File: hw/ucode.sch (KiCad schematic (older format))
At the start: 15 parts, among them U501 74HC393, U502 74HCT02, U503 74HCT02, U504 74HCT238, U505 74HCT238, U506 27C64, U507 27C64, U508 27C64, U509 74HCT175, U510 74HCT175, U511 74HCT175, U512 74HCT175, U513 74HCT175, U514 74HCT175

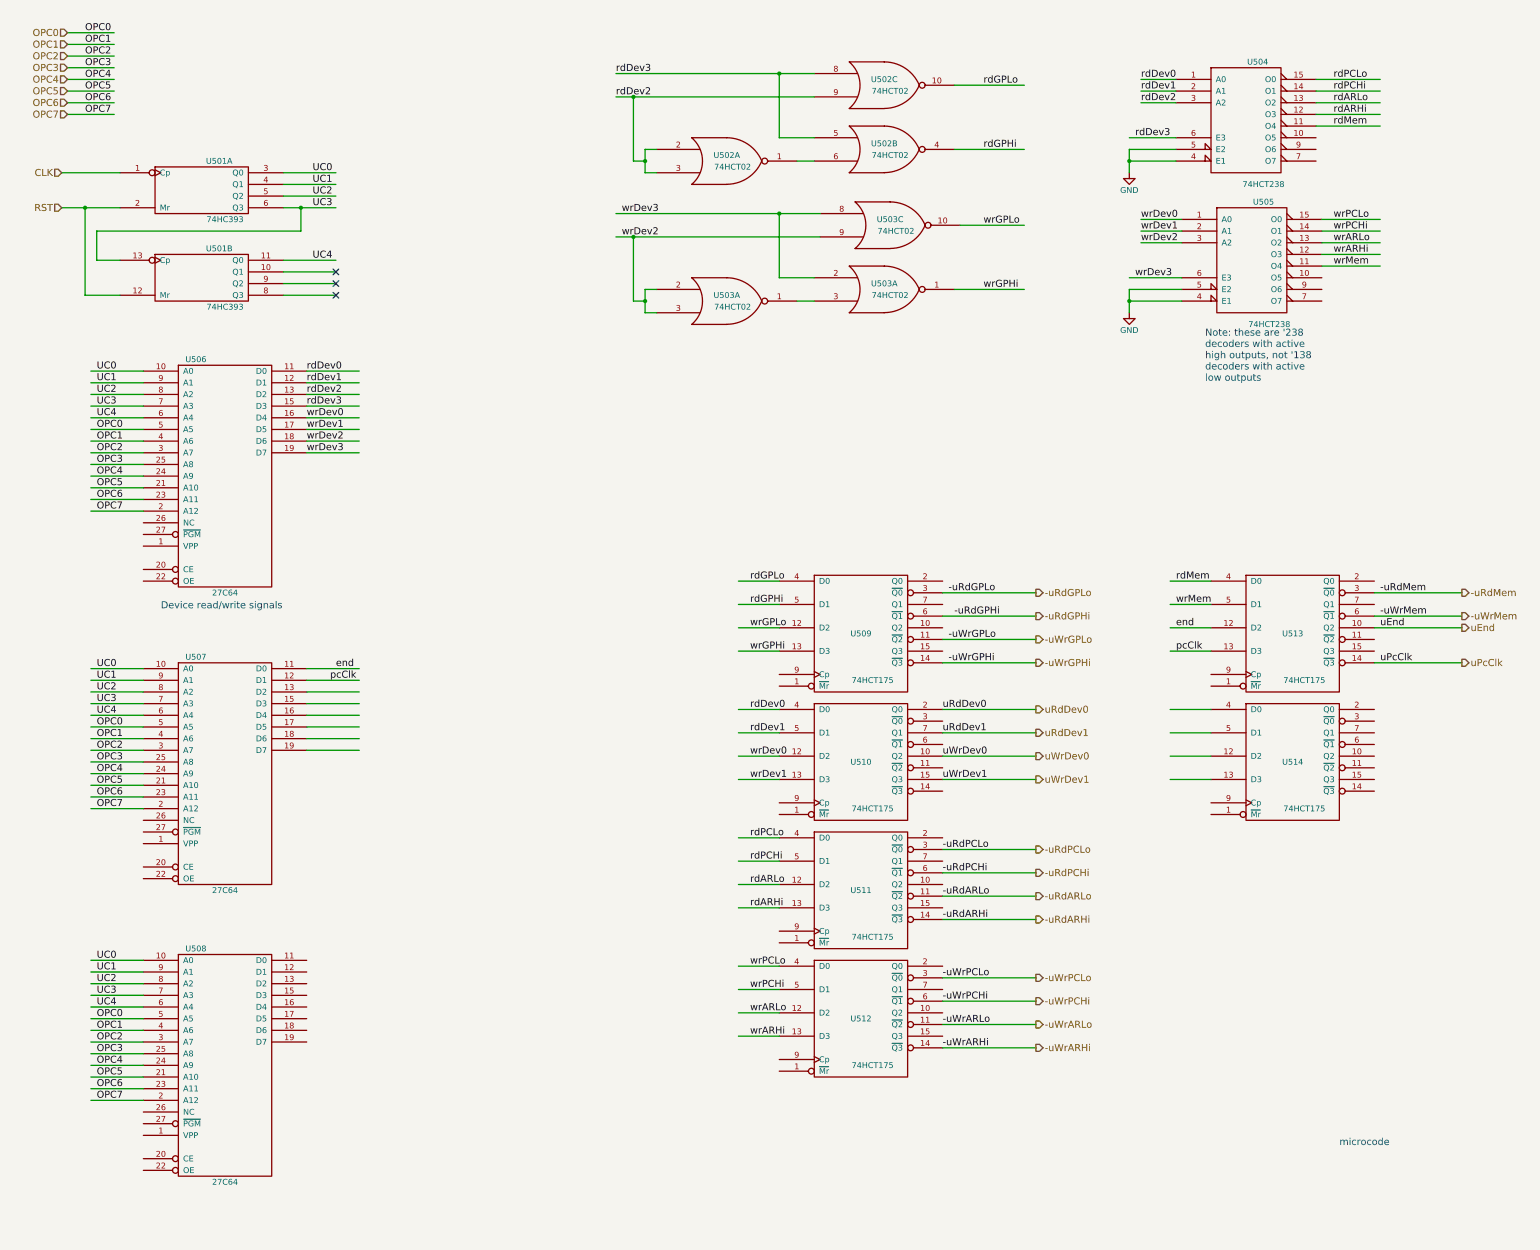
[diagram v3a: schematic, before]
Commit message: added reset/disable logic to ucode, connect CLK
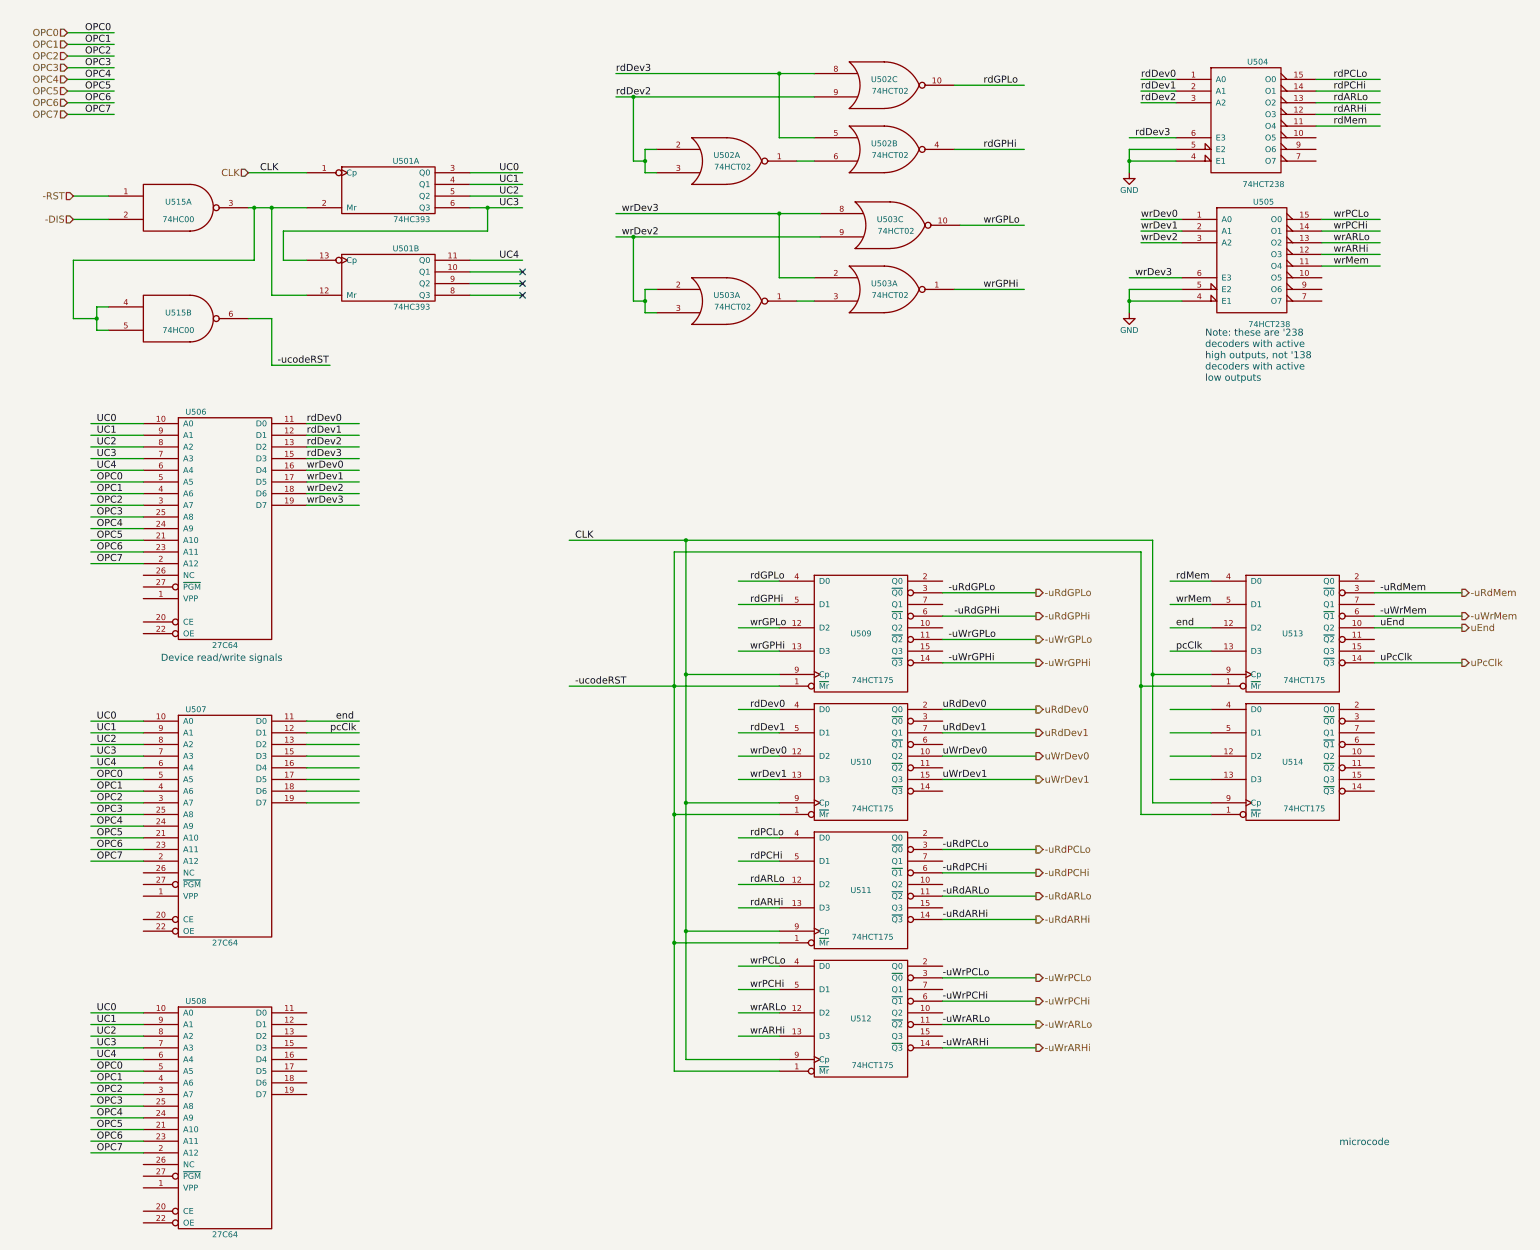
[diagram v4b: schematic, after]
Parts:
- added U515: 74HC00, symbol 74LS00
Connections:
- net labels added: -DIS, -RST, -ucodeRST
- net labels removed: RST
- wire segments 171 -> 201
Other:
- moved on the sheet: U501A, U501B, U506, U507, U508

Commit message: use unused NAND gates as inverters
This means we only need one '02, rather than 2.
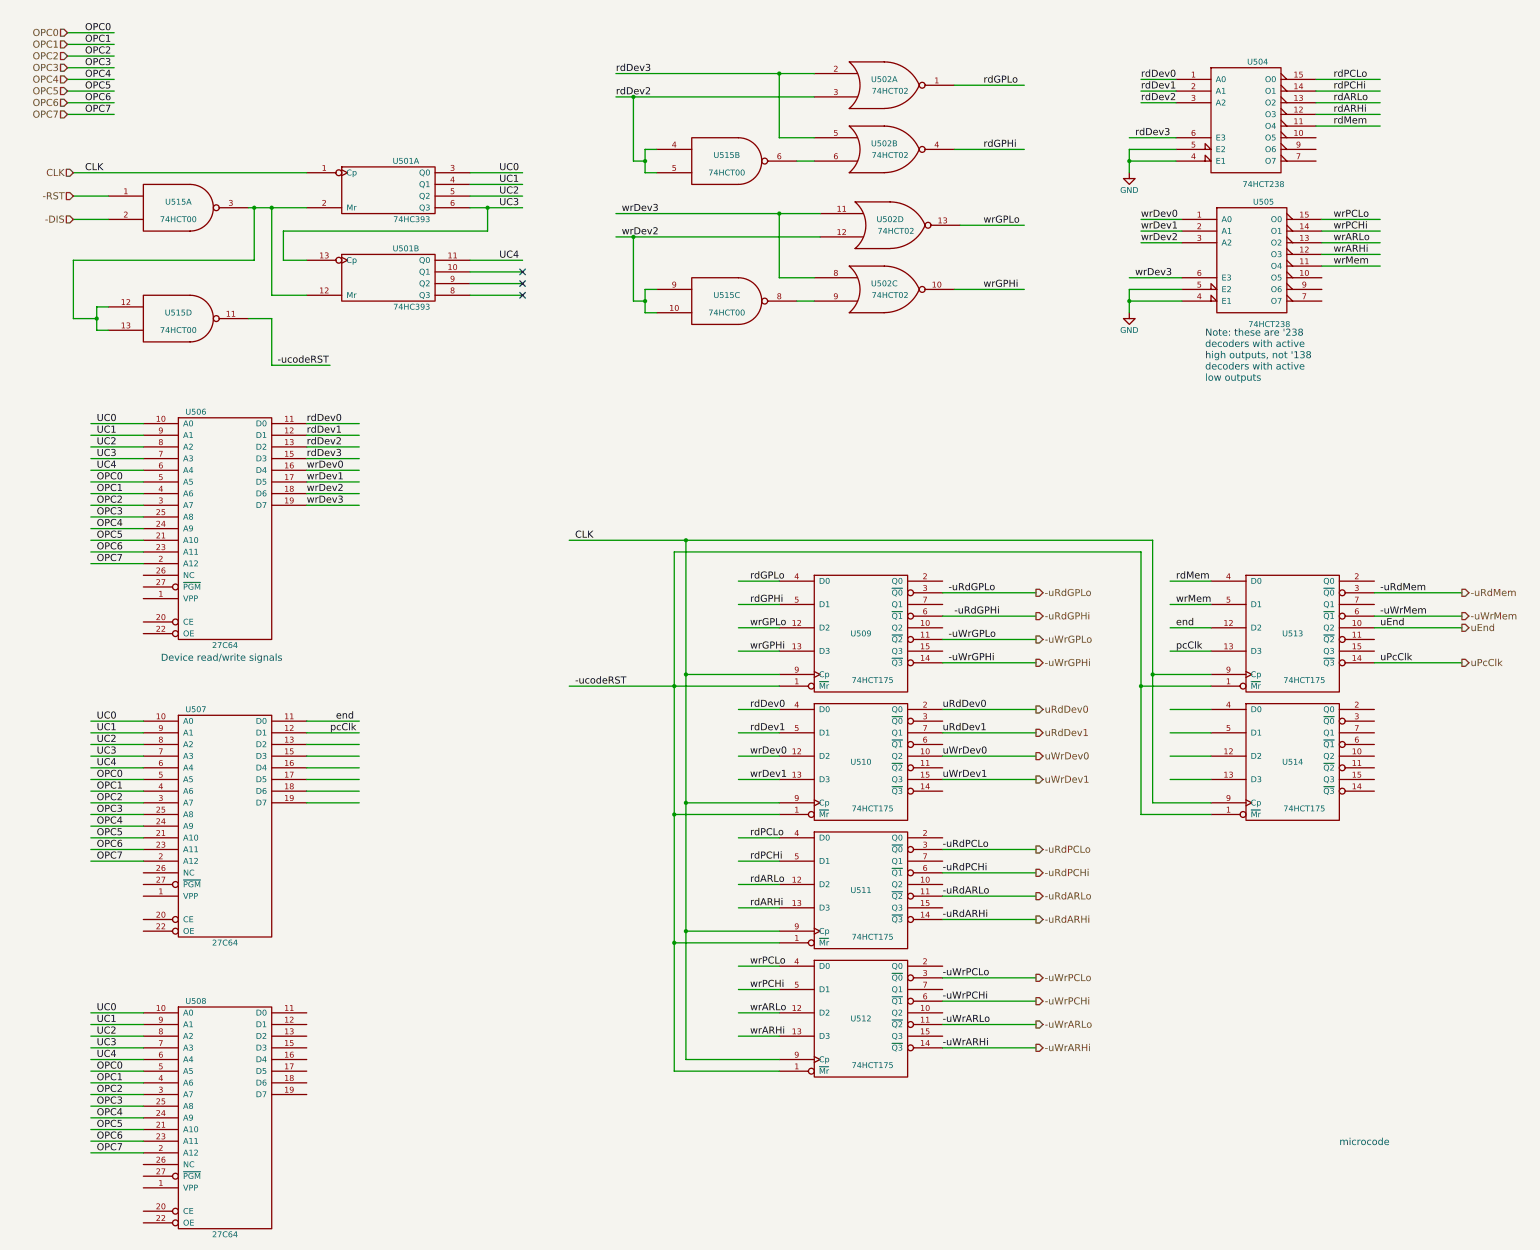
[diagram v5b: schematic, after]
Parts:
- removed unit 1 of U502
- removed U503: 74HCT02, symbol 74LS02
- added unit 2 of U515
- added unit 3 of U515
- U515: value 74HC00 -> 74HCT00
- renumbered U503 to U502
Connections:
- wire segments 201 -> 223
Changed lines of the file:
@@
 Text Notes 11950 10200 0    60   ~ 0
 microcode
-Text HLabel 2600 1850 0    60   Input ~ 0
+Text HLabel 1100 1850 0    60   Input ~ 0
 CLK
 Text Label 3100 4000 0    60   ~ 0
@@
 $Comp
 L 74LS02 U502
-U 3 1 592CB86F
+U 1 1 592CB86F
 P 8050 1100
 F 0 "U502" H 8050 1150 50  0000 C CNN
@@
 F 2 "" H 8050 1100 50  0000 C CNN
 F 3 "" H 8050 1100 50  0000 C CNN
-	3    8050 1100
-	1    0    0    -1
-$EndComp
-$Comp
-L 74LS02 U503
-U 3 1 592CB898
+	1    8050 1100
+	1    0    0    -1
+$EndComp
+$Comp
+L 74LS02 U502
+U 4 1 592CB898
 P 8100 2300
-F 0 "U503" H 8100 2350 50  0000 C CNN
+F 0 "U502" H 8100 2350 50  0000 C CNN
 F 1 "74HCT02" H 8150 2250 50  0000 C CNN
 F 2 "" H 8100 2300 50  0000 C CNN
 F 3 "" H 8100 2300 50  0000 C CNN
-	3    8100 2300
+	4    8100 2300
 	1    0    0    -1
 $EndComp
@@
 $Comp
 L 74LS02 U502
-U 1 1 592CC31B
-P 6700 1750
-F 0 "U502" H 6700 1800 50  0000 C CNN
-F 1 "74HCT02" H 6750 1700 50  0000 C CNN
-F 2 "" H 6700 1750 50  0000 C CNN
-F 3 "" H 6700 1750 50  0000 C CNN
-	1    6700 1750
-	1    0    0    -1
-$EndComp
-$Comp
-L 74LS02 U502
 U 2 1 592CC548
 P 8050 1650
@@
 $EndComp
 $Comp
-L 74LS02 U503
-U 1 1 592CC893
-P 6700 2950
-F 0 "U503" H 6700 3000 50  0000 C CNN
-F 1 "74HCT02" H 6750 2900 50  0000 C CNN
-F 2 "" H 6700 2950 50  0000 C CNN
-F 3 "" H 6700 2950 50  0000 C CNN
-	1    6700 2950
-	1    0    0    -1
-$EndComp
-$Comp
-L 74LS02 U503
-U 1 1 592CC899
+L 74LS02 U502
+U 3 1 592CC899
 P 8050 2850
-F 0 "U503" H 8050 2900 50  0000 C CNN
+F 0 "U502" H 8050 2900 50  0000 C CNN
 F 1 "74HCT02" H 8100 2800 50  0000 C CNN
 F 2 "" H 8050 2850 50  0000 C CNN
 F 3 "" H 8050 2850 50  0000 C CNN
-	1    8050 2850
+	3    8050 2850
 	1    0    0    -1
 $EndComp
@@
 P 2000 2150
 F 0 "U515" H 2000 2200 50  0000 C CNN
-F 1 "74HC00" H 2000 2050 50  0000 C CNN
+F 1 "74HCT00" H 2000 2050 50  0000 C CNN
 F 2 "" H 2000 2150 50  0001 C CNN
 F 3 "" H 2000 2150 50  0001 C CNN
@@
 $Comp
 L 74LS00 U515
-U 2 1 59408AC8
+U 4 1 59408AC8
 P 2000 3100
 F 0 "U515" H 2000 3150 50  0000 C CNN
-F 1 "74HC00" H 2000 3000 50  0000 C CNN
+F 1 "74HCT00" H 2000 3000 50  0000 C CNN
 F 2 "" H 2000 3100 50  0001 C CNN
 F 3 "" H 2000 3100 50  0001 C CNN
-	2    2000 3100
+	4    2000 3100
 	1    0    0    -1
 $EndComp
@@
 	1050 1350 1450 1350
 Wire Wire Line
-	4500 2150 4950 2150
+	4500 2150 4650 2150
+Wire Wire Line
+	4650 2150 4950 2150
 Wire Wire Line
 	4650 2150 4650 2350
@@
 	4500 2900 4950 2900
 Wire Wire Line
-	2600 2150 3100 2150
+	2600 2150 2650 2150
+Wire Wire Line
+	2650 2150 2800 2150
+Wire Wire Line
+	2800 2150 3100 2150
 Wire Wire Line
 	3100 2900 2800 2900
@@
 Connection ~ 2800 2150
 Wire Wire Line
-	2600 1850 3100 1850
+	1100 1850 3100 1850
 Wire Wire Line
 	3100 4000 3550 4000
@@
 	10150 1750 10550 1750
 Wire Wire Line
-	10150 1650 10150 1850
+	10150 1650 10150 1750
+Wire Wire Line
+	10150 1750 10150 1850
 Wire Wire Line
 	10550 1050 10250 1050
@@
 	10600 2950 10150 2950
 Wire Wire Line
-	10150 2850 10150 3050
+	10150 2850 10150 2950
+Wire Wire Line
+	10150 2950 10150 3050
 Wire Wire Line
 	11800 2250 12300 2250
@@
 	11800 2650 12300 2650
 Wire Wire Line
-	5750 1000 7450 1000
-Wire Wire Line
-	5750 1200 7450 1200
-Wire Wire Line
-	5750 2200 7500 2200
-Wire Wire Line
-	5750 2400 7500 2400
+	5750 1000 7150 1000
+Wire Wire Line
+	7150 1000 7450 1000
+Wire Wire Line
+	5750 1200 5900 1200
+Wire Wire Line
+	5900 1200 7450 1200
+Wire Wire Line
+	5750 2200 7150 2200
+Wire Wire Line
+	7150 2200 7500 2200
+Wire Wire Line
+	5750 2400 5900 2400
+Wire Wire Line
+	5900 2400 7500 2400
 Wire Wire Line
 	8650 1100 9250 1100
@@
 Connection ~ 7150 1000
 Wire Wire Line
-	6100 1650 6000 1650
-Wire Wire Line
-	6000 1650 6000 1850
-Wire Wire Line
-	6000 1750 5900 1750
-Wire Wire Line
 	5900 1750 5900 1200
 Connection ~ 5900 1200
 Wire Wire Line
-	6000 1850 6100 1850
-Connection ~ 6000 1750
-Wire Wire Line
 	8650 1650 9250 1650
 Wire Wire Line
@@
 	6100 2850 6000 2850
 Wire Wire Line
-	6000 2850 6000 3050
+	6000 2850 6000 2950
+Wire Wire Line
+	6000 2950 6000 3050
 Wire Wire Line
 	6000 2950 5900 2950
@@
 	1400 3000 1300 3000
 Wire Wire Line
-	1300 3000 1300 3200
+	1300 3000 1300 3100
+Wire Wire Line
+	1300 3100 1300 3200
 Wire Wire Line
 	1300 3100 1100 3100
@@
 -ucodeRST
 Wire Wire Line
-	5350 6250 7150 6250
+	5350 6250 6250 6250
+Wire Wire Line
+	6250 6250 7150 6250
 Text Label 5400 6250 0    60   ~ 0
 -ucodeRST
@@
 	6250 7350 7150 7350
 Wire Wire Line
-	6250 5100 6250 9550
+	6250 5100 6250 6250
+Wire Wire Line
+	6250 6250 6250 7350
+Wire Wire Line
+	6250 7350 6250 8450
+Wire Wire Line
+	6250 8450 6250 9550
 Connection ~ 6250 6250
 Wire Wire Line
@@
 	10850 6250 10250 6250
 Wire Wire Line
-	10250 5100 10250 7350
+	10250 5100 10250 6250
+Wire Wire Line
+	10250 6250 10250 7350
 Wire Wire Line
 	10250 5100 6250 5100
@@
 	10250 7350 10850 7350
 Connection ~ 10250 6250
-Text Label 2700 1850 0    60   ~ 0
+Text Label 1200 1850 0    60   ~ 0
 CLK
 Wire Wire Line
 	7150 6150 6350 6150
 Wire Wire Line
-	6350 5000 6350 9450
-Wire Wire Line
-	5350 5000 10350 5000
+	6350 5000 6350 6150
+Wire Wire Line
+	6350 6150 6350 7250
+Wire Wire Line
+	6350 7250 6350 8350
+Wire Wire Line
+	6350 8350 6350 9450
+Wire Wire Line
+	5350 5000 6350 5000
+Wire Wire Line
+	6350 5000 10350 5000
 Text Label 5400 5000 0    60   ~ 0
 CLK
@@
 	10850 6150 10350 6150
 Wire Wire Line
-	10350 5000 10350 7250
+	10350 5000 10350 6150
+Wire Wire Line
+	10350 6150 10350 7250
 Connection ~ 6350 5000
 Wire Wire Line
 	10350 7250 10850 7250
 Connection ~ 10350 6150
+Connection ~ 6000 1750
+Wire Wire Line
+	6000 1850 6100 1850
+Wire Wire Line
+	6000 1750 5900 1750
+Wire Wire Line
+	6000 1650 6000 1750
+Wire Wire Line
+	6000 1750 6000 1850
+Wire Wire Line
+	6100 1650 6000 1650
+$Comp
+L 74LS00 U515
+U 2 1 59446B0E
+P 6700 1750
+F 0 "U515" H 6700 1800 50  0000 C CNN
+F 1 "74HCT00" H 6700 1650 50  0000 C CNN
+F 2 "" H 6700 1750 50  0001 C CNN
+F 3 "" H 6700 1750 50  0001 C CNN
+	2    6700 1750
+	1    0    0    -1
+$EndComp
+$Comp
+L 74LS00 U515
+U 3 1 59446EB8
+P 6700 2950
+F 0 "U515" H 6700 3000 50  0000 C CNN
+F 1 "74HCT00" H 6700 2850 50  0000 C CNN
+F 2 "" H 6700 2950 50  0001 C CNN
+F 3 "" H 6700 2950 50  0001 C CNN
+	3    6700 2950
+	1    0    0    -1
+$EndComp
 $EndSCHEMATC
